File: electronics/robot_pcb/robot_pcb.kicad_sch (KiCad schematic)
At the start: 0 parts

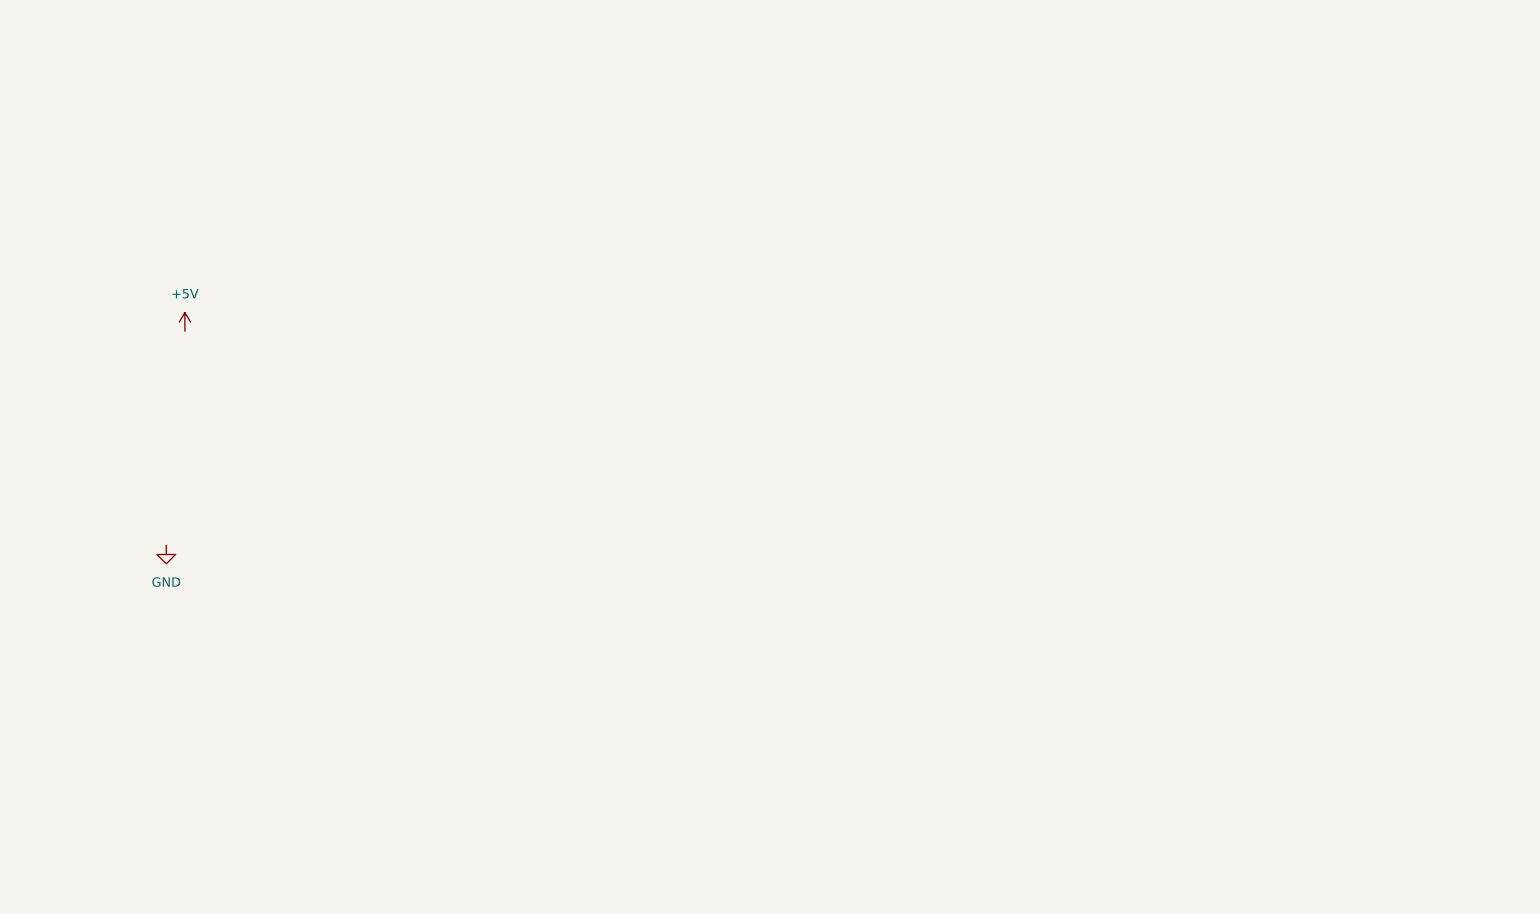
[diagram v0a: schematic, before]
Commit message: Finished ESP32 board schematic
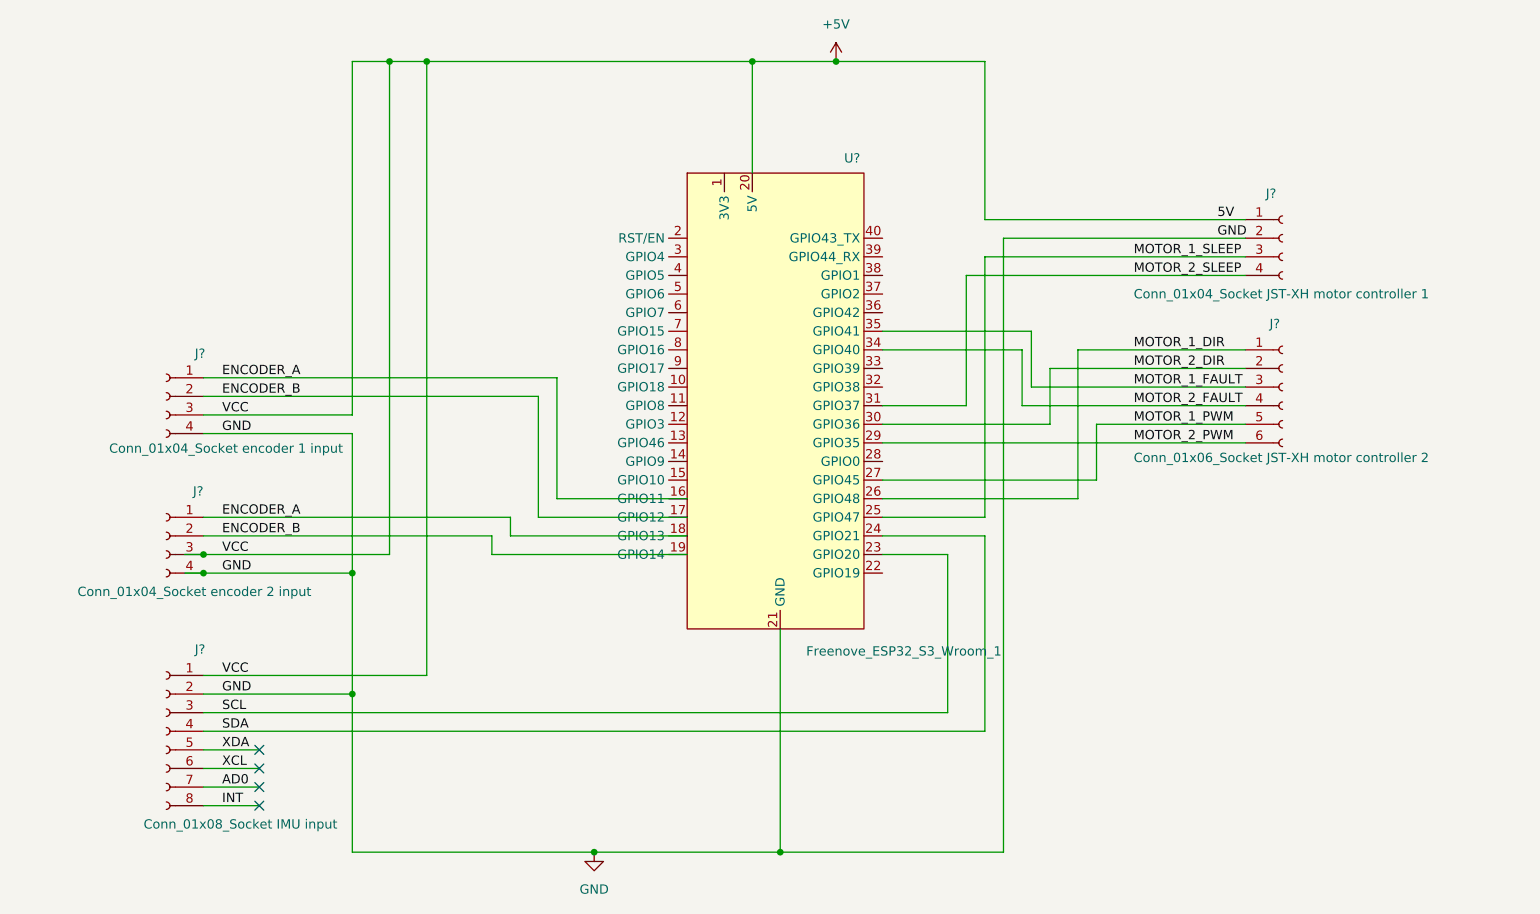
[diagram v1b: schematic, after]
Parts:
- added J?: Conn_01x04_Socket encoder 1 input, symbol Connector:Conn_01x04_Socket
- added J?: Conn_01x04_Socket JST-XH motor controller 1, symbol Connector:Conn_01x04_Socket
- added J?: Conn_01x04_Socket encoder 2 input, symbol Connector:Conn_01x04_Socket
- added J?: Conn_01x08_Socket IMU input, symbol Connector:Conn_01x08_Socket
- added J?: Conn_01x06_Socket JST-XH motor controller 2, symbol Connector:Conn_01x06_Socket
- added U?: Freenove_ESP32_S3_Wroom_1, symbol MCU_Espressif_ESP32:Freenove_ESP32_S3_Wroom_1
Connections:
- net +5V: now also J?.1 (Pin_1), J?.1 (Pin_1), J?.3 (Pin_3), J?.3 (Pin_3), U?.20 (5V)
- net GND: now also J?.2 (Pin_2), J?.2 (Pin_2), J?.4 (Pin_4), J?.4 (Pin_4), U?.21 (GND)
- new net AD0: J?.7 (Pin_7)
- new net ENCODER_A: J?.1 (Pin_1), J?.1 (Pin_1), U?.16 (GPIO11), U?.18 (GPIO13)
- new net ENCODER_B: J?.2 (Pin_2), J?.2 (Pin_2), U?.17 (GPIO12), U?.19 (GPIO14)
- new net INT: J?.8 (Pin_8)
- new net MOTOR_1_DIR: J?.1 (Pin_1), U?.26 (GPIO48)
- new net MOTOR_1_FAULT: J?.3 (Pin_3), U?.35 (GPIO41)
- new net MOTOR_1_PWM: J?.5 (Pin_5), U?.27 (GPIO45)
- new net MOTOR_1_SLEEP: J?.3 (Pin_3), U?.25 (GPIO47)
- new net MOTOR_2_DIR: J?.2 (Pin_2), U?.30 (GPIO36)
- new net MOTOR_2_FAULT: J?.4 (Pin_4), U?.34 (GPIO40)
- new net MOTOR_2_PWM: J?.6 (Pin_6), U?.29 (GPIO35)
- new net MOTOR_2_SLEEP: J?.4 (Pin_4), U?.31 (GPIO37)
- new net SCL: J?.3 (Pin_3), U?.23 (GPIO20)
- new net SDA: J?.4 (Pin_4), U?.24 (GPIO21)
- new net XCL: J?.6 (Pin_6)
- new net XDA: J?.5 (Pin_5)
- no-connect marks 0 -> 4
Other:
- title: (none) -> Self-balancing robot ESP32 board
